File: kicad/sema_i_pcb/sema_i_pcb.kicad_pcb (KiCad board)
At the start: 2 copper layers, 52 x 10 mm, 25 parts, among them SW1 SW_SPDT, U1 PIC24FJ64GA002-E_SO, U2 ESP8266-01_ESP-01, U3 edge_connector

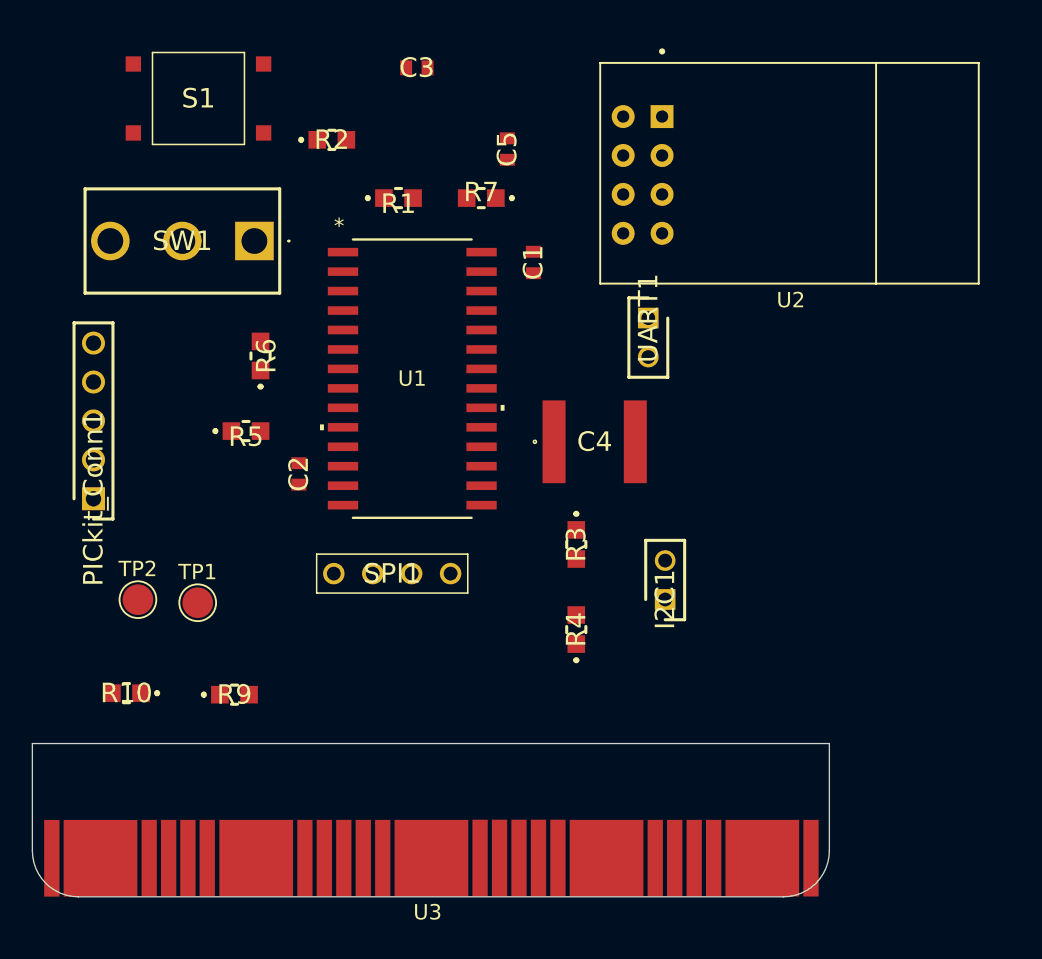
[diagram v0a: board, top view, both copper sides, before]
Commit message: Issue #8 : Rutiranje komponenata na PCB - Dodana rutirana šema
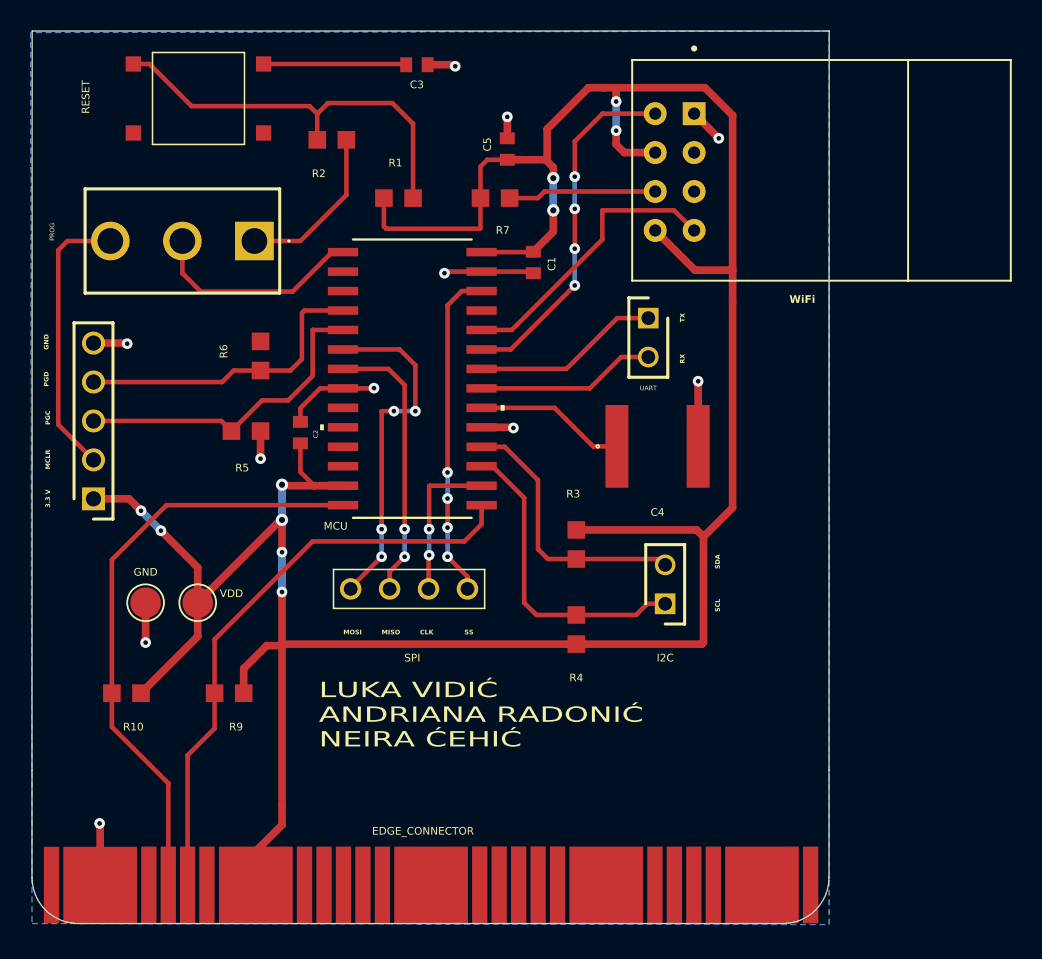
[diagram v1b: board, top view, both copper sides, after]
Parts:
- R1, R5, R6, R7: value 10k -> ERA6AEB1020V
- R2: value 330R -> ERA6AEB1020V
- moved C4 4.11 mm to (143.0, 111.1)
- moved C2 2.70 mm to (119.7, 110.2)
- moved U2 2.10 mm to (153.7, 93.2)
- moved EDGE_CONNECTOR 1.74 mm to (102.2, 142.2)
- moved SPI 1.49 mm to (123.0, 120.4)
- moved R7 0.90 mm to (132.4, 94.9), turned to 0 degrees
- moved GND 0.54 mm to (109.6, 121.3)
- moved R9 0.36 mm to (115.0, 127.2), turned to 180 degrees
- moved I2C 0.28 mm to (143.5, 121.4)
- moved C3 0.20 mm to (127.3, 86.2)
- renumbered U3 to EDGE_CONNECTOR, TP2 to GND, I2C1 to I2C, U1 to MCU, SW1 to PROG, S1 to RESET, SPI1 to SPI, UART1 to UART, TP1 to VDD
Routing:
- net +3.3V: track 0.00 -> 194.3 mm, vias 0 -> 10
- net /SDA_MBIT: track 0.00 -> 39.3 mm
- net /SCL_MBIT: track 0.00 -> 38.7 mm
- net GND: track 0.00 -> 34.7 mm, vias 0 -> 11
- net Net-(R1-Pad2): track 0.00 -> 27.0 mm
- net /SPI_DO: track 0.00 -> 23.3 mm, vias 0 -> 4
- net /UART_TX_WIFI: track 0.00 -> 23.2 mm, vias 0 -> 4
- net /SPI_SS: track 0.00 -> 21.7 mm, vias 0 -> 4
- net /PGC: track 0.00 -> 21.0 mm
- net /I2C_SCL: track 0.00 -> 20.9 mm
- net /PGD: track 0.00 -> 20.0 mm
- net /UART_RX_WIFI: track 0.00 -> 18.8 mm
- net /SPI_DI: track 0.00 -> 18.5 mm, vias 0 -> 2
- net /THROW_PROG: track 0.00 -> 18.3 mm
- net /I2C_SDA: track 0.00 -> 18.0 mm
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- added copper zone on B.Cu, net GND
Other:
- board size 52 x 10 mm -> 52 x 48.2 mm
- board text added: "3.3 V"
- board text added: "CLK"
- board text added: "GND"
- board text added: "LUKA VIDIĆ ANDRIANA RADONIĆ NEIRA ĆEHIĆ"
- board text added: "MCLR"
- board text added: "MISO"
- board text added: "MOSI"
- board text added: "PGC"
- board text added: "PGD"
- board text added: "RX"
- board text added: "SCL"
- board text added: "SDA"
- board text added: "SS"
- board text added: "TX"
- board text added: "WiFi"

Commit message: Globalne izmjene:
- Promjenjena odabrana komponenta 10uF kondenzatora
- Ažurirani otisak i 3D model novog kondenzatora
- Popravljene greške u PCB u vezi sa silkscreen-om i zaostalim vezama
- Izmjene silkscreen-a na drugim otiscima komponenti
- Blage dorade u dizajnu štampane ploče
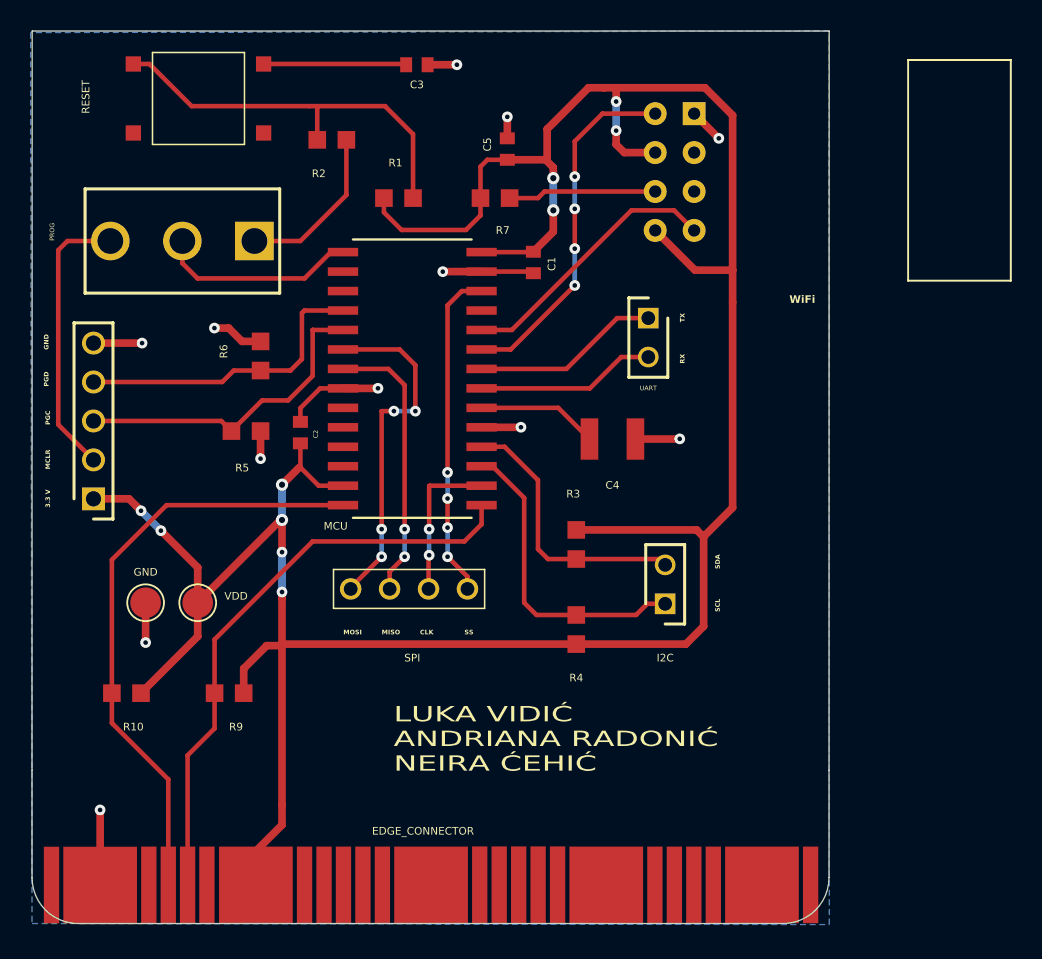
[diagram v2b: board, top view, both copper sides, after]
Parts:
- moved C4 2.98 mm to (140.1, 110.6)
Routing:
- net GND: track 34.7 -> 39.3 mm, vias 11 -> 12
- net +3.3V: track 194.3 -> 190.9 mm
- net Net-(U1-VCAP/VDDCORE): track 9.87 -> 7.88 mm
- net /UART_RX_WIFI: track 18.8 -> 17.6 mm
- net /MCLR: track 14.1 -> 13.0 mm
